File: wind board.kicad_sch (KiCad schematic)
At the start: 59 parts, among them J1 USB_C_Receptacle_USB2.0_14P, J2 Conn_01x06_MountingPin, J3 Conn_01x06_MountingPin, U1 CH334R, U2 FT232RL, U3 FT232RL, U4 ZT3222F, U5 ZT3222F, Y1 12MHz

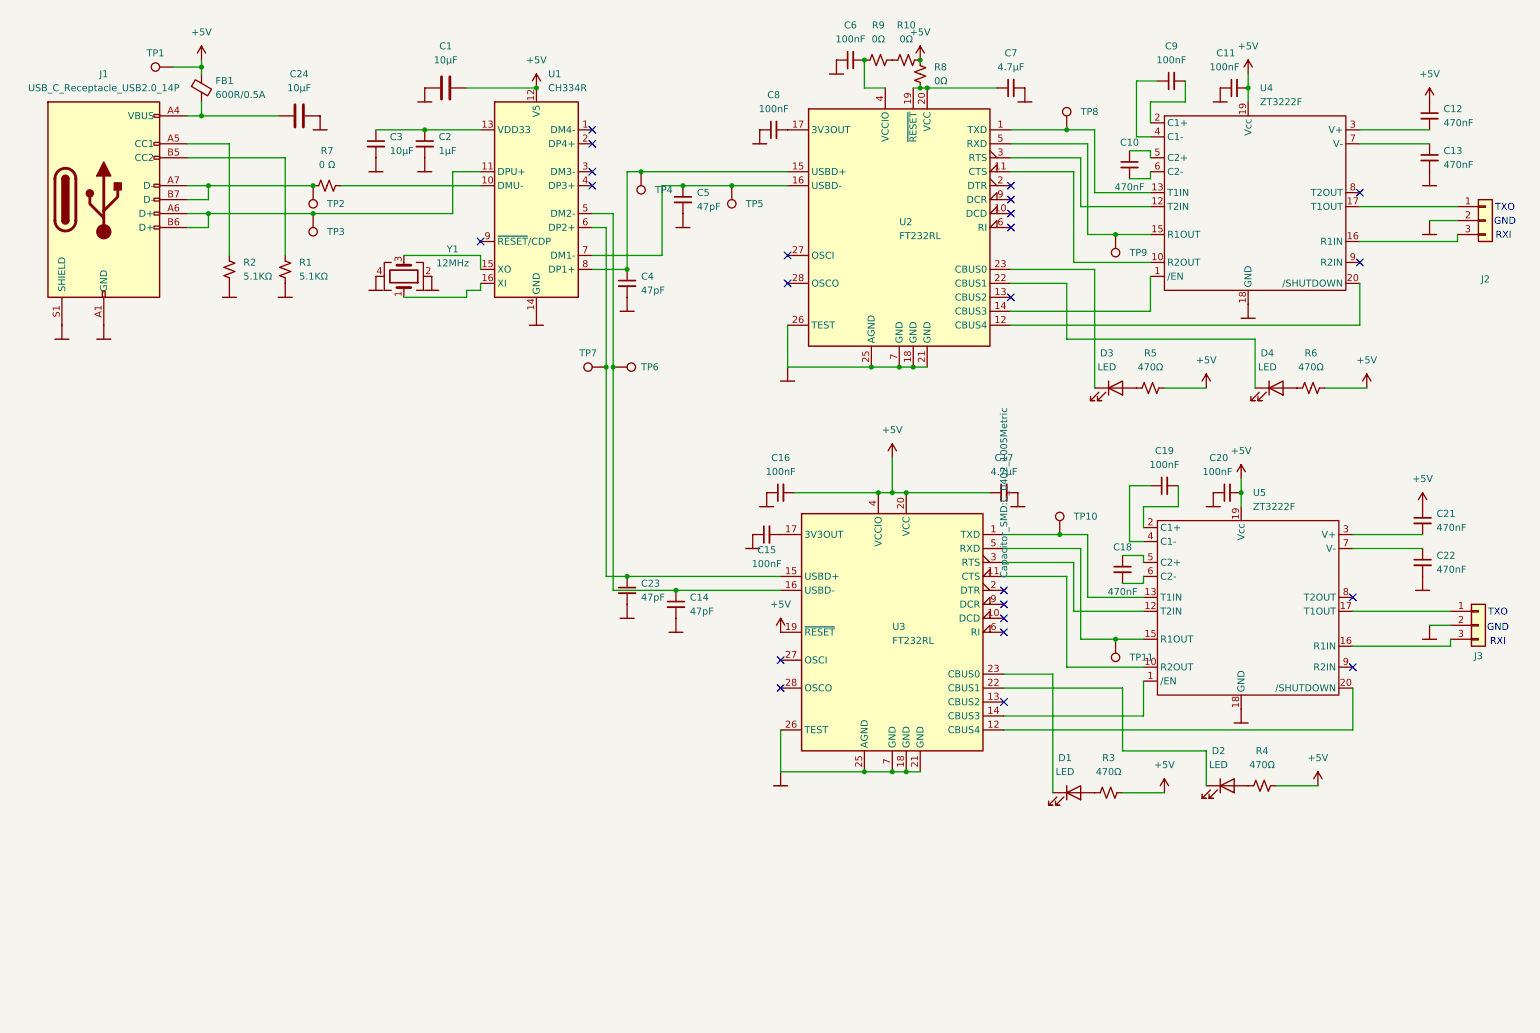
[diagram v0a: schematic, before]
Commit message: added 3rd interface, tvs diodes, charging circuit
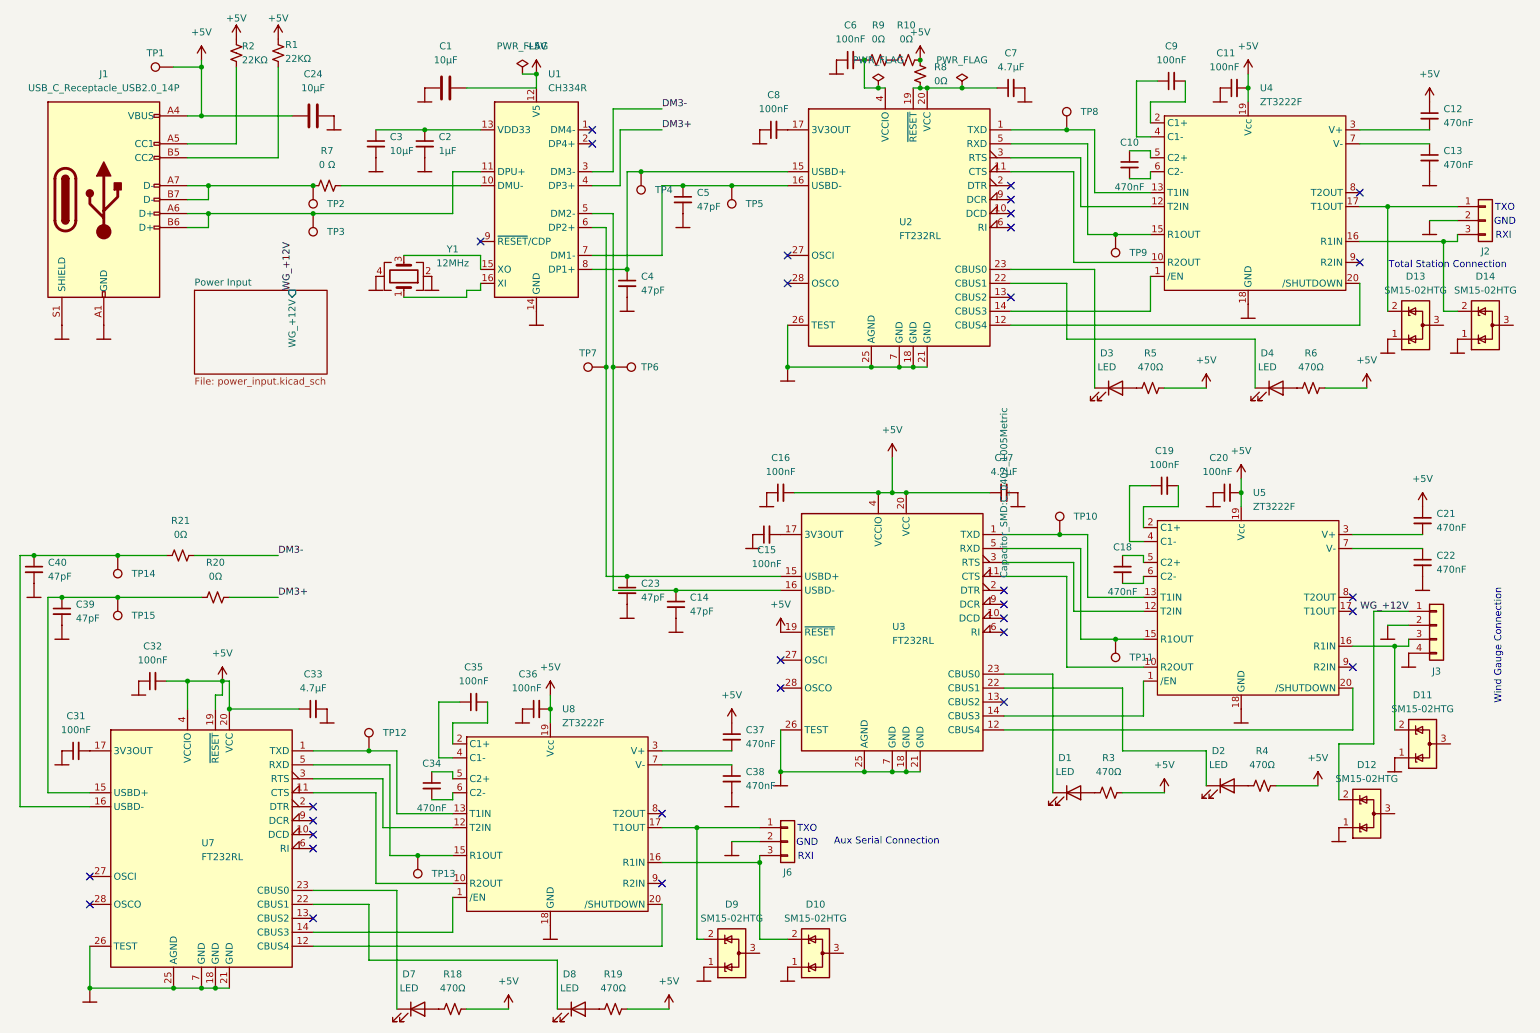
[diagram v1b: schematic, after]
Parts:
- removed FB1: 600R/0.5A, Inductor_SMD:L_0805_2012Metric, symbol Device:FerriteBead_Small
- added C31, C32, C35, C36: 100nF, Capacitor_SMD:C_0402_1005Metric, symbol Device:C_Small
- added C33: 4.7µF, Capacitor_SMD:C_0603_1608Metric, symbol Device:C_Small
- added C34, C37, C38: 470nF, Capacitor_SMD:C_0603_1608Metric, symbol Device:C_Small
- added C39, C40: 47pF, Capacitor_SMD:C_0402_1005Metric, symbol Device:C_Small
- added D10, D11, D12, D13, D14, D9: SM15-02HTG, Package_TO_SOT_SMD:SM0502HTG, symbol Power_Protection:ESDA5V3L
- added D7, D8: LED, LED_SMD:LED_0805_2012Metric, symbol Device:LED
- added J6: Conn_01x06_MountingPin, Connector_PinHeader_2.54mm:PinHeader_1x03_P2.54mm_Vertical, symbol Connector_Generic:Conn_01x03
- added R18, R19: 470Ω, Resistor_SMD:R_0603_1608Metric, symbol Device:R_Small_US
- added R20, R21: 0Ω, Resistor_SMD:R_0402_1005Metric, symbol Device:R_Small_US
- added TP12, TP13, TP14, TP15: TestPoint, TestPoint:TestPoint_Pad_1.0x1.0mm, symbol Connector:TestPoint
- added U7: FT232RL, Package_SO:SSOP-28_5.3x10.2mm_P0.65mm, symbol Interface_USB:FT232RL
- added U8: ZT3222F, Package_SO:TSSOP-20_4.4x6.5mm_P0.65mm, symbol Interface_UART:ZT3222F_1
- C7: footprint Capacitor_SMD:C_0402_1005Metric -> Capacitor_SMD:C_0603_1608Metric
- J3: footprint Connector_PinHeader_2.54mm:PinHeader_1x03_P2.54mm_Vertical -> Connector_PinHeader_2.54mm:PinHeader_1x04_P2.54mm_Vertical; symbol Connector_Generic:Conn_01x03 -> Connector_Generic:Conn_01x04
- R1, R2: value 5.1KΩ -> 22KΩ
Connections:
- net +5V: now also C24.1, J1.A4 (VBUS), J1.A9 (VBUS), J1.B4 (VBUS), J1.B9 (VBUS), R1.1, R2.1, C32.2, C33.1, C36.2, C37.1, R18.2, R19.2, U7.19 (~{RESET}), U7.20 (VCC), U7.4 (VCCIO), U8.19 (Vcc)
- net at J1.A5 (CC1): now also R2.2; no longer R2.1
- net at J1.B5 (CC2): now also R1.2; no longer R1.1
- net at U5.17 (T1OUT): no longer J3.1 (Pin_1)
- net at J3.3 (Pin_3), U5.16 (R1IN): now also D11.2 (K)
- net DM3-: now reaches U1.3 (DM3-)
- net DM3-: now also R21.1
- net DM3+: now reaches U1.4 (DP3+)
- net DM3+: now also R20.1
- net at J2.3 (Pin_3), U4.16 (R1IN): now also D14.2 (K)
- net at J2.1 (Pin_1), U4.17 (T1OUT): now also D13.2 (K)
- new net: D9.2 (K), J6.1 (Pin_1), U8.17 (T1OUT)
- new net: D10.2 (K), J6.3 (Pin_3), U8.16 (R1IN)
- new net: TP12.1, U7.1 (TXD), U8.13 (T1IN)
- new net: U7.14 (CBUS3), U8.1 (/EN)
- new net: U7.11 (CTS), U8.10 (R2OUT)
- new net: U7.3 (RTS), U8.12 (T2IN)
- new net: TP13.1, U7.5 (RXD), U8.15 (R1OUT)
- new net: C35.2, U8.2 (C1+)
- new net: U7.12 (CBUS4), U8.20 (/SHUTDOWN)
- new net: C37.2, U8.3 (V+)
- new net: C35.1, U8.4 (C1-)
- new net: C34.1, U8.5 (C2+)
- new net: C34.2, U8.6 (C2-)
- new net: C38.1, U8.7 (V-)
- new net: C31.2, U7.17 (3V3OUT)
- new net: D7.2 (A), R18.1
- new net: C40.1, R21.2, TP14.1, U7.16 (USBD-)
- new net: D7.1 (K), U7.23 (CBUS0)
- new net: C39.1, R20.2, TP15.1, U7.15 (USBD+)
- new net: D8.1 (K), U7.22 (CBUS1)
- new net: D8.2 (A), R19.1
- new net: U7.18 (GND), U7.21 (GND), U7.25 (AGND), U7.26 (TEST), U7.7 (GND)
- new net WG_+12V: D12.2 (K), J3.1 (Pin_1)
- no-connect marks 23 -> 31
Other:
- added sheet Power Input (power_input.kicad_sch)
- note added: "Aux Serial Connection"
- note added: "Total Station Connection"
- note added: "Wind Gauge Connection"
- moved on the sheet: C24, R1, R2

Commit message: latest
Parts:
- removed R10, R20, R21, R8, R9: 0Ω, Resistor_SMD:R_0402_1005Metric, symbol Device:R_Small_US
- removed R7: 0 Ω, Resistor_SMD:R_0603_1608Metric, symbol Device:R_Small_US
- C1, C24, C3: value 10µF -> 10uF
- C17, C33, C7: value 4.7µF -> 4.7uF
- C2: value 1µF -> 1uF
- R1, R2: value 22KΩ -> 22K
- R18, R19, R3, R4, R5, R6: value 470Ω -> 470
- TP1, TP10, TP11, TP12, TP13, TP14, TP15, TP2, TP3, TP4, TP5, TP6, TP7, TP8, TP9: footprint TestPoint:TestPoint_Pad_1.0x1.0mm -> TestPoint:TestPoint_THTPad_1.0x1.0mm_Drill0.5mm
- U2, U3, U7: value FT232RL -> FT232RNL
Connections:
- net +5V: now also C6.2, C7.1, U2.19 (~{RESET}), U2.20 (VCC), U2.4 (VCCIO)
- net DM3+: now also C39.1, TP15.1, U7.15 (USBD+)
- net DM3-: now also C40.1, TP14.1, U7.16 (USBD-)
- net at J1.A7 (D-), J1.B7 (D-), TP2.1: now also U1.10 (DMU-)
- net at C4.1, TP4.1, U2.15 (USBD+): now also U1.6 (DP2+); no longer U1.8 (DP1+)
- net at C23.1, TP7.1, U3.15 (USBD+): now also U1.8 (DP1+); no longer U1.6 (DP2+)
- net at C5.1, TP5.1, U2.16 (USBD-): now also U1.5 (DM2-); no longer U1.7 (DM1-)
- net at C14.1, TP6.1, U3.16 (USBD-): now also U1.7 (DM1-); no longer U1.5 (DM2-)

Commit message: starting pd chip
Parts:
- removed C24: 10uF, Capacitor_SMD:C_0603_1608Metric, symbol Device:C
- removed J1: USB_C_Receptacle_USB2.0_14P, Connector_USB:USB_C_Receptacle_HRO_TYPE-C-31-M-12, symbol Connector:USB_C_Receptacle_USB2.0_14P
- removed R1, R2: 22K, Resistor_SMD:R_0603_1608Metric, symbol Device:R_Small_US
- removed TP2, TP3: TestPoint, TestPoint:TestPoint_THTPad_1.0x1.0mm_Drill0.5mm, symbol Connector:TestPoint
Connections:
- net USB_C_PD/DP+: now reaches U1.11 (DPU+)
- net USB_C_PD/DM-: now reaches U1.10 (DMU-)
- net at C2.1, C3.1: no longer U1.13 (VDD33)
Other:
- added sheet USB_C_PD (USB_C_PD.kicad_sch)
- moved on the sheet: C2, C3, TP1

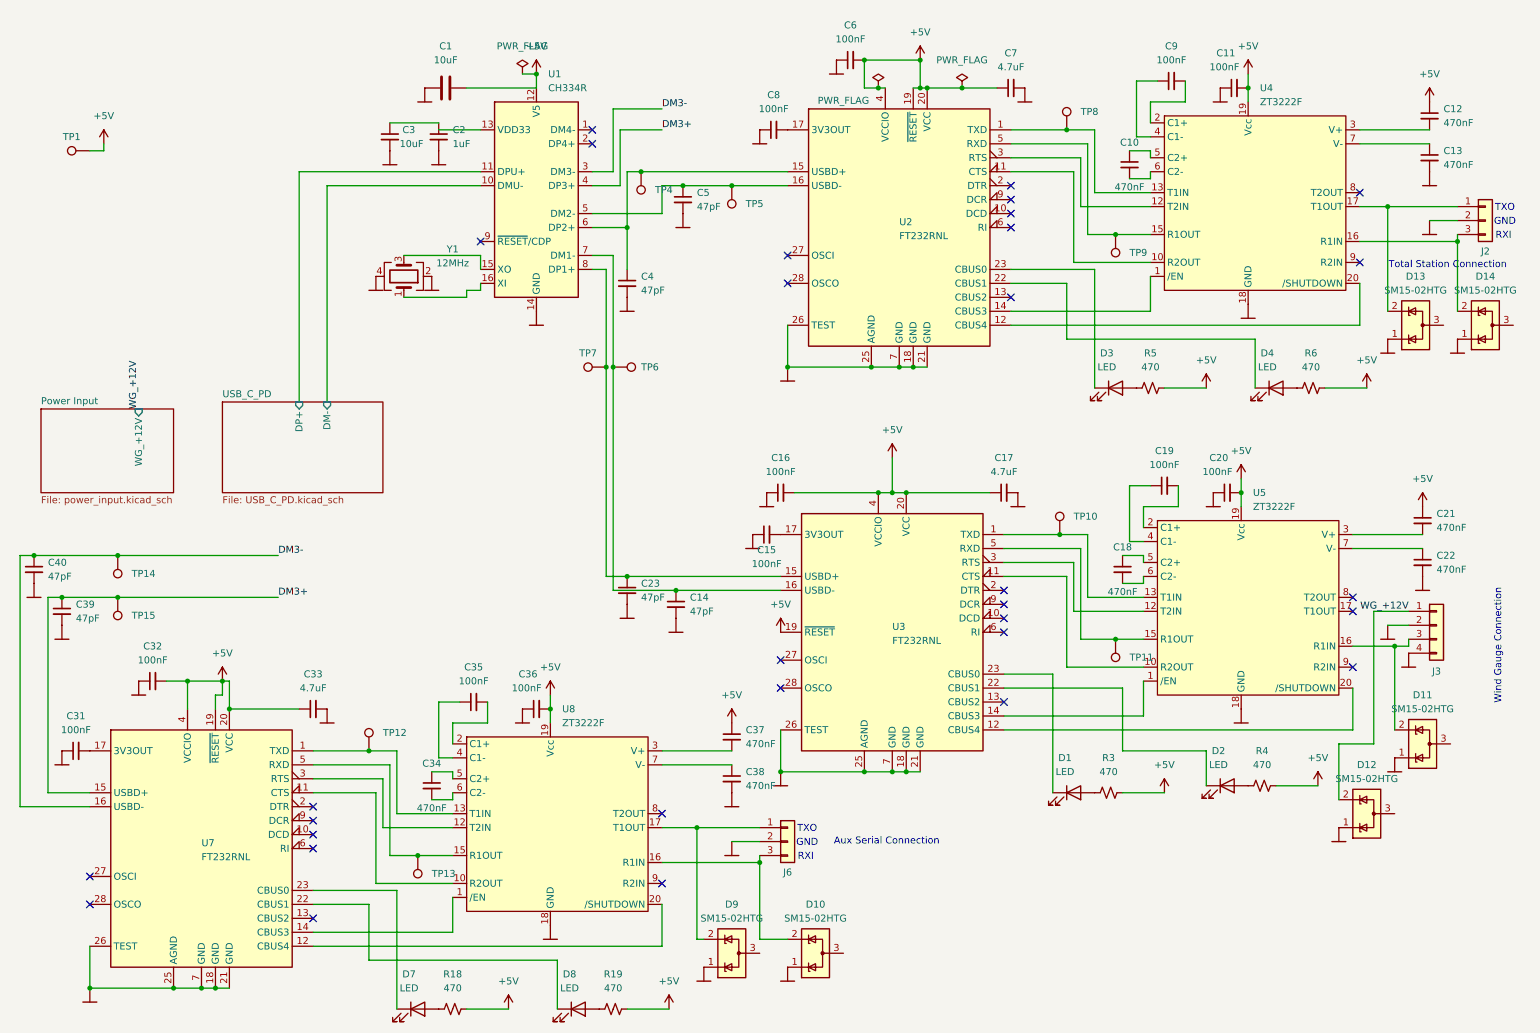
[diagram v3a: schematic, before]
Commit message: add usb-c-pd routing
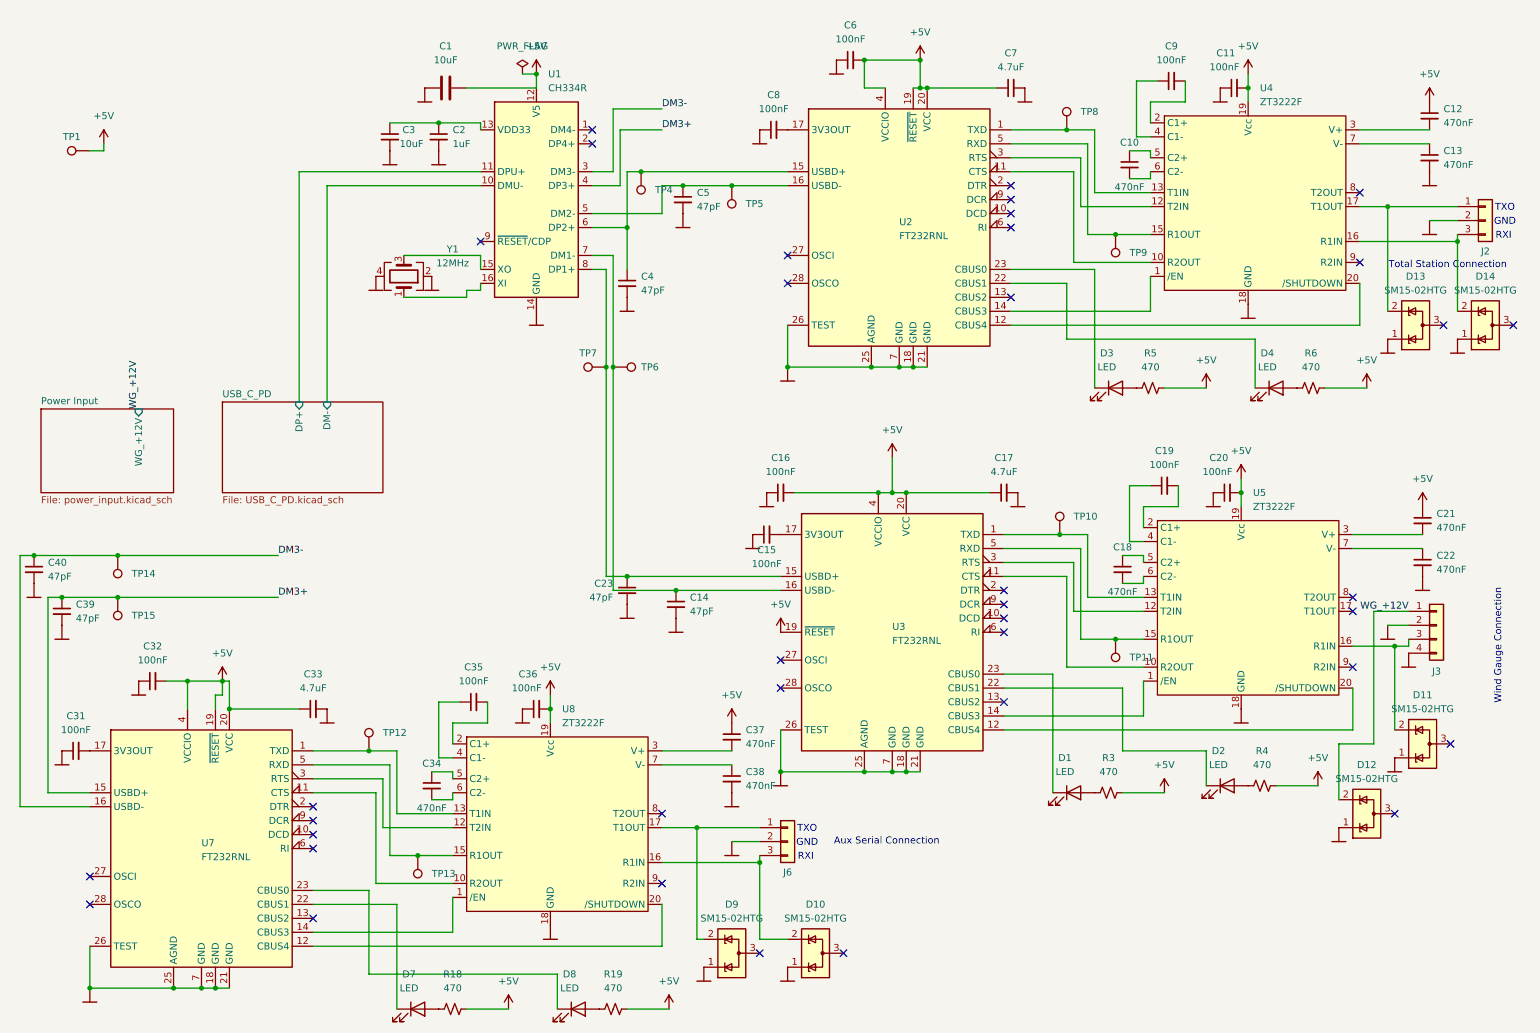
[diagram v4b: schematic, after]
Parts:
- C1, C2, C3: footprint Capacitor_SMD:C_0603_1608Metric -> Capacitor_SMD:C_0402_1005Metric
- D1, D2, D3, D4, D7, D8: footprint LED_SMD:LED_0805_2012Metric -> LED_SMD:LED_0603_1608Metric
- R18, R19, R3, R4, R5, R6: footprint Resistor_SMD:R_0603_1608Metric -> Resistor_SMD:R_0402_1005Metric
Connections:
- net at D7.1 (K): now also U7.22 (CBUS1); no longer U7.23 (CBUS0)
- net at D8.1 (K): now also U7.23 (CBUS0); no longer U7.22 (CBUS1)
- net at C2.1, C3.1: now also U1.13 (VDD33)
- no-connect marks 31 -> 37

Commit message: update bom
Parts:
- J2, J6: footprint Connector_PinHeader_2.54mm:PinHeader_1x03_P2.54mm_Vertical -> Connector_PinHeader_2.54mm:PinHeader_1x03_P2.54mm_Horizontal
- J3: footprint Connector_PinHeader_2.54mm:PinHeader_1x04_P2.54mm_Vertical -> Connector_PinHeader_2.54mm:PinHeader_1x04_P2.54mm_Horizontal
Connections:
- net at D9.2 (K), U8.17 (T1OUT): now also J6.3 (Pin_3); no longer J6.1 (Pin_1)
- net at D10.2 (K), U8.16 (R1IN): now also J6.1 (Pin_1); no longer J6.3 (Pin_3)
- net at D14.2 (K), U4.16 (R1IN): now also J2.1 (Pin_1); no longer J2.3 (Pin_3)
- net at D13.2 (K), U4.17 (T1OUT): now also J2.3 (Pin_3); no longer J2.1 (Pin_1)
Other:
- moved on the sheet: J6
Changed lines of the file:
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@@
 	(wire
 		(pts
+			(xy 148.59 167.64) (xy 147.32 167.64)
+		)
+		(stroke
+			(width 0)
+			(type default)
+		)
+	)
+	(wire
+		(pts
 			(xy 172.72 77.47) (xy 175.26 77.47)
 		)
@@
 	(wire
 		(pts
-			(xy 142.24 163.83) (xy 147.32 163.83)
+			(xy 142.24 163.83) (xy 148.59 163.83)
 		)
 		(stroke
@@
 	(wire
 		(pts
-			(xy 147.32 167.64) (xy 147.32 166.37)
+			(xy 148.59 167.64) (xy 148.59 166.37)
 		)
 		(stroke
@@
 	(wire
 		(pts
-			(xy 212.09 53.34) (xy 218.44 53.34)
+			(xy 78.74 161.29) (xy 91.44 161.29)
 		)
 		(stroke
@@
 	(wire
 		(pts
-			(xy 166.37 21.59) (xy 176.53 21.59)
+			(xy 212.09 53.34) (xy 218.44 53.34)
 		)
 		(stroke
@@
 	(wire
 		(pts
-			(xy 152.4 41.91) (xy 125.73 41.91)
+			(xy 166.37 21.59) (xy 176.53 21.59)
 		)
 		(stroke
@@
 	(wire
 		(pts
-			(xy 207.01 53.34) (xy 212.09 53.34)
+			(xy 152.4 41.91) (xy 125.73 41.91)
 		)
 		(stroke
@@
 	(wire
 		(pts
-			(xy 223.52 102.87) (xy 223.52 99.06)
+			(xy 207.01 53.34) (xy 212.09 53.34)
 		)
 		(stroke
@@
 	(wire
 		(pts
-			(xy 135.89 161.29) (xy 147.32 161.29)
+			(xy 223.52 102.87) (xy 223.52 99.06)
 		)
 		(stroke
@@
 	(wire
 		(pts
-			(xy 78.74 161.29) (xy 91.44 161.29)
+			(xy 135.89 161.29) (xy 148.59 161.29)
 		)
 		(stroke
@@
 			)
 		)
-		(property "Footprint" "Connector_PinHeader_2.54mm:PinHeader_1x04_P2.54mm_Vertical"
+		(property "Footprint" "Connector_PinHeader_2.54mm:PinHeader_1x04_P2.54mm_Horizontal"
 			(at 270.51 124.46 0)
 			(effects
@@
 	(symbol
 		(lib_id "Connector_Generic:Conn_01x03")
-		(at 152.4 163.83 0)
+		(at 153.67 163.83 0)
+		(mirror x)
 		(unit 1)
 		(exclude_from_sim no)
@@
 		(dnp no)
 		(property "Reference" "J6"
-			(at 152.4 169.418 0)
+			(at 153.67 158.242 0)
 			(effects
 				(font
@@
 		)
 		(property "Value" "Conn_01x06_MountingPin"
-			(at 133.35 180.848 0)
+			(at 134.62 146.812 0)
 			(effects
 				(font
@@
 			)
 		)
-		(property "Footprint" "Connector_PinHeader_2.54mm:PinHeader_1x03_P2.54mm_Vertical"
-			(at 152.4 163.83 0)
+		(property "Footprint" "Connector_PinHeader_2.54mm:PinHeader_1x03_P2.54mm_Horizontal"
+			(at 153.67 163.83 0)
 			(effects
 				(font
@@
 		)
 		(property "Datasheet" "~"
-			(at 152.4 163.83 0)
+			(at 153.67 163.83 0)
 			(effects
 				(font
@@
 		)
 		(property "Description" "Generic connector, single row, 01x03, script generated (kicad-library-utils/schlib/autogen/connector/)"
-			(at 152.4 163.83 0)
+			(at 153.67 163.83 0)
 			(effects
 				(font
@@
 		(lib_id "Connector_Generic:Conn_01x03")
 		(at 279.4 50.8 0)
+		(mirror x)
 		(unit 1)
 		(exclude_from_sim no)
@@
 		(dnp no)
 		(property "Reference" "J2"
-			(at 279.4 56.388 0)
+			(at 279.4 45.212 0)
 			(effects
 				(font
@@
 		)
 		(property "Value" "Conn_01x06_MountingPin"
-			(at 260.35 67.818 0)
+			(at 260.35 33.782 0)
 			(effects
 				(font
@@
 			)
 		)
-		(property "Footprint" "Connector_PinHeader_2.54mm:PinHeader_1x03_P2.54mm_Vertical"
+		(property "Footprint" "Connector_PinHeader_2.54mm:PinHeader_1x03_P2.54mm_Horizontal"
 			(at 279.4 50.8 0)
 			(effects
